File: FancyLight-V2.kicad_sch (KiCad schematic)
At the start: 40 parts, among them J1 PWR, Q1 IRLML2402, SW1 ONOFF, U1 SB6286, U2 TP4056, U3 TTP223-BA6, U4 DW01-P, U5 CJL8205A

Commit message: WIP
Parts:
- removed C6: 10pF (15pF), Capacitor_SMD:C_0805_2012Metric, symbol Device:C_Small
- removed C7: 0.1u, Capacitor_SMD:C_0805_2012Metric, symbol Device:C_Small
- removed J1: PWR, Connector_USB:USB_Micro-B_Molex_47346-0001, symbol Connector:USB_B_Micro
- removed R10: 470, Resistor_SMD:R_0805_2012Metric, symbol Device:R_Small
- removed R12: 100, Resistor_SMD:R_0805_2012Metric, symbol Device:R_Small
- removed R13: 1k, Resistor_SMD:R_0805_2012Metric, symbol Device:R_Small
- removed TP1: VBAT, TestPoint:TestPoint_Pad_1.5x1.5mm, symbol Connector:TestPoint
- removed TP2: GND, TestPoint:TestPoint_Pad_1.5x1.5mm, symbol Connector:TestPoint
- removed TP3: TOGGLE, TestPoint:TestPoint_Pad_1.5x1.5mm, symbol Connector:TestPoint
- removed TP4: SENSE, TestPoint:TestPoint_Pad_1.0x1.0mm, symbol Connector:TestPoint
- removed U3: TTP223-BA6, Package_TO_SOT_SMD:SOT-23-6, symbol TTP223-BA6:TTP223-BA6
- removed U4: DW01-P, Package_TO_SOT_SMD:SOT-23-6, symbol glebko:DW01-P
- removed U5: CJL8205A, Package_TO_SOT_SMD:TSOT-23-6, symbol glebko:CJL8205A
- added C3: 0.1u, Capacitor_SMD:C_0603_1608Metric, symbol Device:C_Small
- added D10: LED, LED_SMD:LED_0603_1608Metric, symbol Device:LED
- added D7, D8: MBR0520LT1, Diode_SMD:D_SOD-123, symbol Device:D_Schottky
- added D9: RB751V-40, Diode_SMD:D_SOD-323, symbol Device:D_Schottky
- added H1, H2, H3, H4: ~, MountingHole:MountingHole_2.5mm, symbol Mechanical:MountingHole
- added J2: TOUCH, Connector_PinHeader_1.27mm:PinHeader_1x03_P1.27mm_Vertical, symbol Connector:Conn_01x03_Pin
- added J2: ISP, Connector_PinHeader_2.54mm:PinHeader_2x03_P2.54mm_Vertical, symbol Connector_Generic:Conn_02x03_Odd_Even
- added J3: MODE, Connector_PinHeader_2.54mm:PinHeader_2x02_P2.54mm_Vertical, symbol Connector_Generic:Conn_02x02_Odd_Even
- added Q2: IRLML2402, Package_TO_SOT_SMD:SOT-23, symbol Device:Q_NMOS_GSD
- added R15: R_Photo, Connector_PinHeader_1.27mm:PinHeader_1x02_P1.27mm_Vertical, symbol Device:R_Photo
- added R17: 5k, Resistor_SMD:R_0603_1608Metric, symbol Device:R_Small
- added R2 (x3): 10k, Resistor_SMD:R_0603_1608Metric, symbol Device:R_Small
- added R2 (x2): 330, Resistor_SMD:R_0603_1608Metric, symbol Device:R_Small
- added RN1: 330, Resistor_SMD:R_Array_Convex_4x0603, symbol Device:R_Pack04
- added U3: XB3303A, kicad_lceda:SOT-23-3_L2.9-W1.3-P1.90-LS2.4-BR, symbol kicad_lceda:XB3303A
- added U5: syn480r, Connector_PinHeader_1.27mm:PinHeader_1x03_P1.27mm_Vertical, symbol rf:syn480r
- added U6: ATtiny44A-M, Package_DFN_QFN:QFN-20-1EP_4x4mm_P0.5mm_EP2.6x2.6mm, symbol MCU_Microchip_ATtiny:ATtiny44A-M
- added USB1: TYPE-C_6P, kicad_lceda:TYPE-C-SMD_TYPE-C-6P, symbol kicad_lceda:TYPE-C_6P
- BT1, SW1: footprint Connector_PinHeader_2.54mm:PinHeader_2x01_P2.54mm_Vertical -> Connector_PinHeader_1.27mm:PinHeader_1x02_P1.27mm_Vertical
- C3, C4: footprint Capacitor_SMD:C_0805_2012Metric -> Capacitor_SMD:C_0603_1608Metric
- C5: footprint Capacitor_SMD:C_0805_2012Metric -> Capacitor_SMD:C_0603_1608Metric; LCSC C49678 -> C15850
- D6: footprint LED_SMD:LED_1206_3216Metric -> LED_SMD:LED_0805_2012Metric
- R11, R3, R4, R5, R6: footprint Resistor_SMD:R_0805_2012Metric -> Resistor_SMD:R_0603_1608Metric
- R7: value 0 -> 5.1k; footprint Resistor_SMD:R_0805_2012Metric -> Resistor_SMD:R_0603_1608Metric; LCSC C304488 -> (none)
- R8: value 0 -> 1k; footprint Resistor_SMD:R_0805_2012Metric -> Resistor_SMD:R_0603_1608Metric; LCSC (none) -> C17513; now fitted; now in the parts list
- R9: value 0 -> 1k; footprint Resistor_SMD:R_0805_2012Metric -> Resistor_SMD:R_0603_1608Metric; LCSC C304488 -> C17513
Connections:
- net BAT+: now also R8.1, D8.2 (A); no longer SW1.1 (A)
- net GND: now also R7.2, R9.1, C3.1, D10.1 (K), J2.2 (Pin_2), J2.6 (Pin_6), Q2.2 (S), R2.1, U3.1 (VM), U6.21 (GND), U6.8 (GND), USB1.7 (EH), USB1.A12 (GND), USB1.B12 (GND); no longer C5.2, R9.2
- net VBAT: now also C3.2, J2.1 (Pin_1), J2.2 (Pin_2), R15.1, R2.2, U5.3 (VCC), U6.9 (VCC); no longer C5.1, R7.2, R8.1
- net PWM: now reaches Q1.1 (G), R11.1
- net PWM: now also RN1.6 (R3.2)
- net at R8.2: now also C5.1, U3.2 (VDD); no longer R9.1
- net at R7.1: now also USB1.A5 (CC1), USB1.B5 (CC2)
- net at BT1.2 (-): now also C5.2, U3.3 (GND)
- net TOGGLE renamed DCDC_EN
- net DCDC_EN: now also RN1.8 (R1.2)
- net VCC: no longer names the net of C3.1, D6.2 (A), U2.4 (VCC), U2.8 (CE)
- net VCC: now also R9.2, D7.2 (A), D9.2 (A), USB1.A9 (VBUS), USB1.B9 (VBUS)
- new net: D10.2 (A), R17.2
- new net: J3.2 (Pin_2), J3.4 (Pin_4), R2.2
- new net: Q2.3 (D), U5.1 (GND)
- new net: RN1.1 (R1.1), U6.5 (AREF/PA0)
- new net: RN1.2 (R2.1), U6.4 (PA1)
- new net: RN1.3 (R3.1), U6.3 (PA2)
- new net: RN1.4 (R4.1), U6.15 (PA7)
- new net: D7.1 (K), D8.1 (K), SW1.1 (A)
- new net: R2.1, U6.12 (XTAL2/PB1)
- new net: R15.2, R2.1, U6.2 (PA3)
- new net MISO: J2.1 (Pin_1), R2.2, U6.20 (PA5)
- new net MODE1: J2.4 (Pin_4), J3.1 (Pin_1), U6.16 (PA6)
- new net MODE2: J3.3 (Pin_3), U6.11 (XTAL1/PB0)
- new net RST: J2.5 (Pin_5), R2.1, U6.13 (~{RESET}/PB3)
- new net R_EN: Q2.1 (G), R2.1
- new net R_TRIG: RN1.5 (R4.2), U5.2 (DAT)
- new net SCK: J2.3 (Pin_3), R17.1, U6.1 (PA4)
- new net SENSE: D9.1 (K), R2.2
- new net SINK: R2.2, U6.14 (PB2)
- new net TRIG: J2.3 (Pin_3), RN1.7 (R2.2)
- no-connect marks 7 -> 1
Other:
- note removed: "P = U * I P = 6.4 * 0.084 = 0.54 Pd = I^2 * Rds Pd = 0.007 * 0.35 = 0.0025"
- note removed: "Vf = 3.2V If = 60 mA (max) Irec = If * 0.7 = 42 mA"
- moved on the sheet: BT1, C4, D1, D2, D3, D4, D6, Q1, R1, R11, R2, R6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

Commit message: Update CAD files and gitignore
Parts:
- J2, J3, L1, R15, USB1: now not fitted; now left out of the parts list
- U5: now left out of the parts list
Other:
- note added: "REMAP PWM PINs!!!!"
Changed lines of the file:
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@@
     (stroke (width 0) (type default))
+  )
+  (text "REMAP PWM PINs!!!!" (at 145.415 92.075 0)
+    (effects (font (size 2 2) (color 255 19 36 1)) (justify left bottom))
   )
   (text "400 mA\n" (at 24.765 121.285 0)
@@
   )
   (symbol (lib_id "LQH32MN2R2K23L:LQH32MN2R2K23L") (at 52.07 155.575 0) (unit 1)
-    (in_bom yes) (on_board yes) (dnp no) (fields_autoplaced)
+    (in_bom no) (on_board yes) (dnp yes) (fields_autoplaced)
     (property "Reference" "L1" (at 52.07 149.86 0)
       (effects (font (size 1.27 1.27)))
@@
   )
   (symbol (lib_id "rf:syn480r") (at 269.875 142.24 0) (unit 1)
-    (in_bom yes) (on_board yes) (dnp yes) (fields_autoplaced)
+    (in_bom no) (on_board yes) (dnp yes) (fields_autoplaced)
     (property "Reference" "U5" (at 270.51 132.08 0)
       (effects (font (size 1.27 1.27)))
@@
   )
   (symbol (lib_id "kicad_lceda:TYPE-C_6P") (at 30.48 61.595 0) (mirror y) (unit 1)
-    (in_bom yes) (on_board yes) (dnp no)
+    (in_bom no) (on_board yes) (dnp yes)
     (property "Reference" "USB1" (at 27.94 50.165 0)
       (effects (font (size 1.27 1.27)))
@@
   )
   (symbol (lib_id "Connector:Conn_01x03_Pin") (at 202.565 19.685 90) (mirror x) (unit 1)
-    (in_bom yes) (on_board yes) (dnp no)
+    (in_bom no) (on_board yes) (dnp yes)
     (property "Reference" "J2" (at 202.565 15.24 90)
       (effects (font (size 1.27 1.27)))
@@
   )
   (symbol (lib_id "Device:R_Photo") (at 270.51 48.895 0) (unit 1)
-    (in_bom yes) (on_board yes) (dnp no) (fields_autoplaced)
+    (in_bom no) (on_board yes) (dnp yes) (fields_autoplaced)
     (property "Reference" "R15" (at 273.05 48.26 0)
       (effects (font (size 1.27 1.27)) (justify left))
@@
   )
   (symbol (lib_id "Connector_Generic:Conn_02x03_Odd_Even") (at 151.13 177.546 0) (unit 1)
-    (in_bom yes) (on_board yes) (dnp no) (fields_autoplaced)
+    (in_bom no) (on_board yes) (dnp yes) (fields_autoplaced)
     (property "Reference" "J2" (at 152.4 169.926 0)
       (effects (font (size 1.27 1.27)))
@@
   )
   (symbol (lib_id "Connector_Generic:Conn_02x02_Odd_Even") (at 273.05 111.76 0) (unit 1)
-    (in_bom yes) (on_board yes) (dnp no) (fields_autoplaced)
+    (in_bom no) (on_board yes) (dnp yes) (fields_autoplaced)
     (property "Reference" "J3" (at 274.32 106.045 0)
       (effects (font (size 1.27 1.27)))

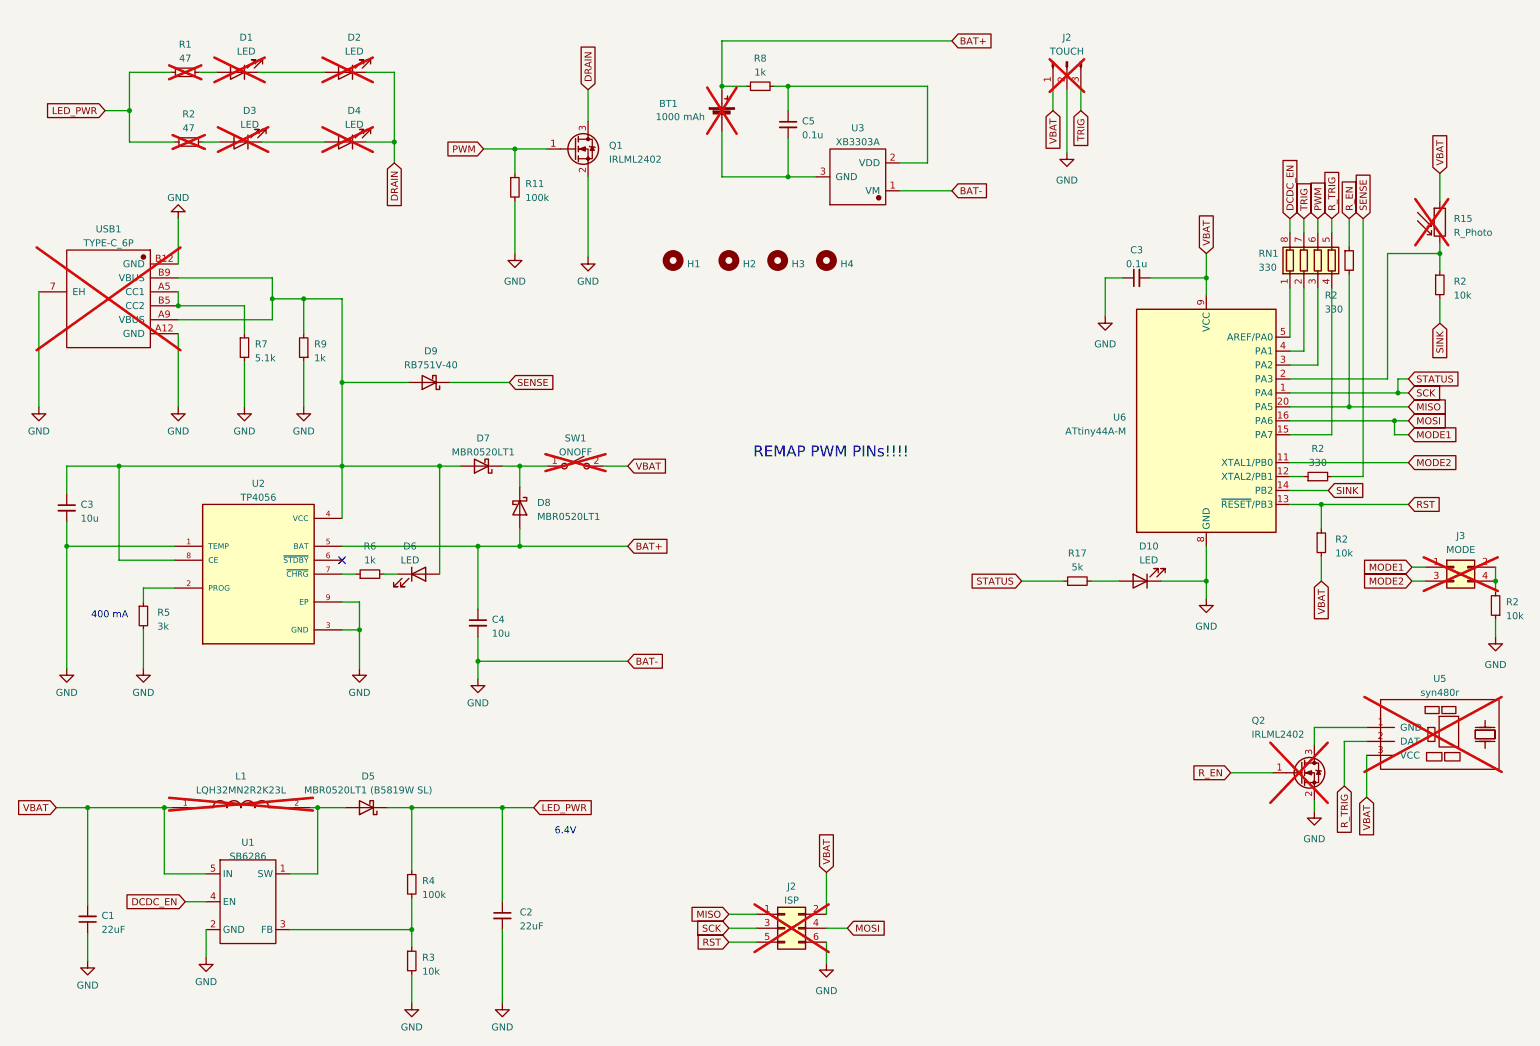
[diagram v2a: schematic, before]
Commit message: feat: Add power control, config, touch control, brightness control, and illumination control modules
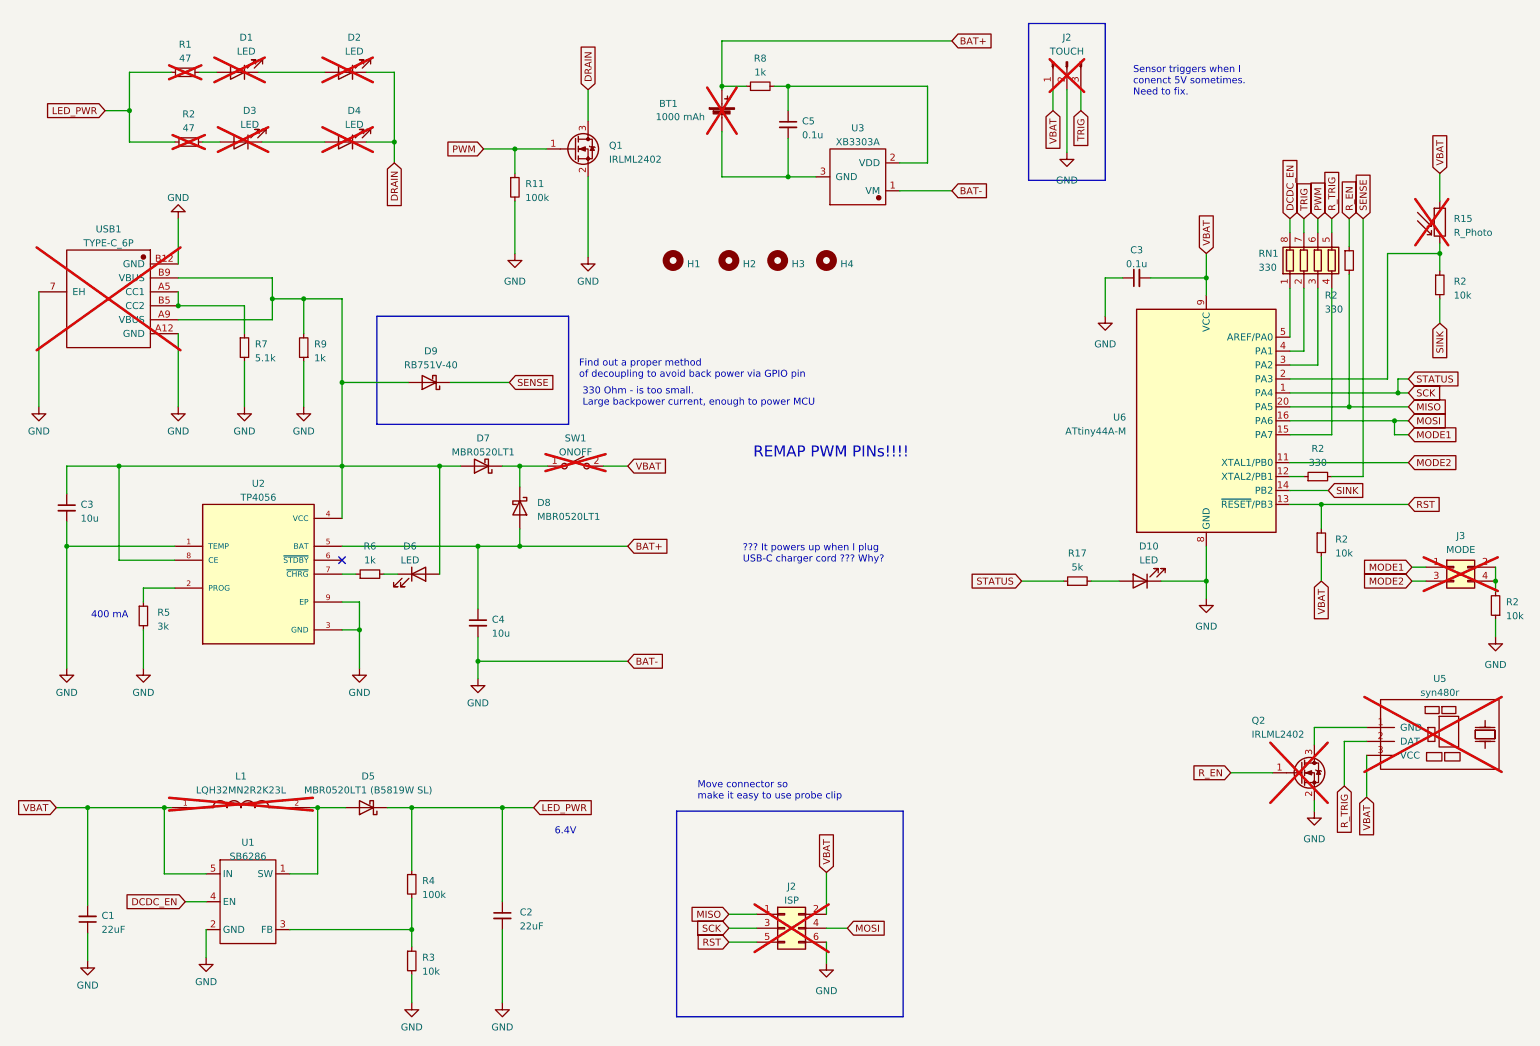
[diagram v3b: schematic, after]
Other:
- note added: "330 Ohm - is too small. Large backpower current, enough to power MCU"
- note added: "??? It powers up when I plug USB-C charger cord ??? Why?"
- note added: "Find out a proper method of decoupling to avoid back power via GPIO pin"
- note added: "Move connector so make it easy to use probe clip"
- note added: "Sensor triggers when I conenct 5V sometimes. Need to fix."
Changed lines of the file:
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@@
     (stroke (width 0) (type default))
+  )
+  (rectangle (start 195.58 12.7) (end 209.55 41.275)
+    (stroke (width 0) (type default))
+    (fill (type none))
+  )
+  (rectangle (start 76.835 66.04) (end 111.76 85.725)
+    (stroke (width 0) (type default))
+    (fill (type none))
+  )
+  (rectangle (start 131.445 156.21) (end 172.72 193.675)
+    (stroke (width 0) (type default))
+    (fill (type none))
+  )
+  (text "330 Ohm - is too small.\nLarge backpower current, enough to power MCU"
+    (at 114.3 82.55 0)
+    (effects (font (size 1.27 1.27)) (justify left bottom))
   )
   (text "REMAP PWM PINs!!!!" (at 145.415 92.075 0)
     (effects (font (size 2 2) (color 255 19 36 1)) (justify left bottom))
+  )
+  (text "Find out a proper method\nof decoupling to avoid back power via GPIO pin"
+    (at 113.665 77.47 0)
+    (effects (font (size 1.27 1.27)) (justify left bottom))
+  )
+  (text "??? It powers up when I plug \nUSB-C charger cord ??? Why?"
+    (at 143.51 111.125 0)
+    (effects (font (size 1.27 1.27)) (justify left bottom))
+  )
+  (text "Move connector so \nmake it easy to use probe clip" (at 135.255 154.305 0)
+    (effects (font (size 1.27 1.27)) (justify left bottom))
   )
   (text "400 mA\n" (at 24.765 121.285 0)
@@
     (effects (font (size 1.27 1.27)) (justify left bottom))
   )
+  (text "Sensor triggers when I\nconenct 5V sometimes.\nNeed to fix."
+    (at 214.63 26.035 0)
+    (effects (font (size 1.27 1.27)) (justify left bottom))
+  )

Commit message: Improve schematic and PCB
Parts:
- removed J2: ISP, Connector_PinHeader_2.54mm:PinHeader_2x03_P2.54mm_Vertical, symbol Connector_Generic:Conn_02x03_Odd_Even
- removed L1: LQH32MN2R2K23L, lib:IND_LQH32MN2R2K23L, symbol LQH32MN2R2K23L:LQH32MN2R2K23L
- removed R2: 330, Resistor_SMD:R_0603_1608Metric, symbol Device:R_Small
- added C5, C7, C8: 10u, Capacitor_SMD:C_0603_1608Metric, symbol Device:C_Small
- added H5: ~, MountingHole:MountingHole_2.1mm, symbol Mechanical:MountingHole
- added J1: ISP, Connector_PinHeader_2.54mm:PinHeader_2x03_P2.54mm_Vertical, symbol Connector_Generic:Conn_02x03_Odd_Even
- added Q1: AO3400A, Package_TO_SOT_SMD:SOT-23, symbol Device:Q_NMOS_GSD
- added R10, R11: 10k, Resistor_SMD:R_0603_1608Metric, symbol Device:R_Small
- added U1: APSWPA3015S4R7MTF, kicad_lceda:IND-SMD_L3.0-W3.0, symbol kicad_lceda:APSWPA3015S4R7MTF
- added U5: HT7530S_C5451677, kicad_lceda:SOT-23-3_L2.9-W1.3-P1.90-LS2.4-BR-CW, symbol kicad_lceda:HT7530S_C5451677
- C1: renamed from C3; LCSC C15850 -> C96446
- C2: renamed from C1; LCSC C398931 -> C45783
- C3: renamed from C4; LCSC C15850 -> C96446
- C3: LCSC (none) -> C14663
- C4: renamed from C2; LCSC C398931 -> C45783
- C6: renamed from C5; LCSC C15850 -> C14663
- D1, D4: LCSC (none) -> C210310; now fitted; now in the parts list
- D10: value LED -> STATUS LED; LCSC (none) -> C2286
- D2: renamed from D3; LCSC (none) -> C210310; now fitted; now in the parts list
- D3: renamed from D2; LCSC (none) -> C210310; now fitted; now in the parts list
- D5: value MBR0520LT1 (B5819W SL) -> B5819W SL
- D6: renamed from D9; value RB751V-40 -> 1N5819WS; LCSC (none) -> C191023
- D7: renamed from D6; value LED -> CHRG LED; footprint LED_SMD:LED_0805_2012Metric -> LED_SMD:LED_0603_1608Metric; LCSC C688886 -> C2286
- D8: renamed from D7; value MBR0520LT1 -> B5819W SL; LCSC (none) -> C8598
- D9: renamed from D8; value MBR0520LT1 -> B5819W SL; LCSC (none) -> C8598
- H1, H2, H3, H4: now not fitted; now left out of the parts list
- Q2: renamed from Q1; value IRLML2402 -> AO3400A; LCSC C5364307 -> C20917
- Q3: renamed from Q2; value IRLML2402 -> AO3400A; LCSC C5364307 -> C20917
- R1: renamed from R5; LCSC C17661 -> C4211
- R12: renamed from R8; LCSC C17513 -> C21190
- R13: renamed from R17; LCSC C17513 -> C23186
- R2: renamed from R1; value 47 -> 22; LCSC (none) -> C17561; now fitted; now in the parts list
- R2: LCSC (none) -> C25804
- R2: LCSC (none) -> C23138
- R3: renamed from R2; value 47 -> 22; LCSC (none) -> C17561; now fitted; now in the parts list
- R4: renamed from R7; LCSC (none) -> C23186
- R5: renamed from R9; LCSC C17513 -> C21190
- R6: LCSC C17513 -> C21190
- R7: renamed from R4; LCSC C149504 -> C25803
- R8: renamed from R3; LCSC C17414 -> C25804
- R9: renamed from R11; LCSC C149504 -> C25803
- RN1: value 330 -> 470; LCSC (none) -> C25510
- U4: renamed from U3; LCSC (none) -> C154937
- U6: LCSC (none) -> C123718
- USB1: LCSC (none) -> C456012; now fitted; now in the parts list
- renumbered R15 to R16, U1 to U2, U2 to U3, U5 to U7
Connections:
- net GND: now also C5.2, C7.2, C8.2, J1.6 (Pin_6), R11.2, U5.1 (GND)
- net MISO: now also J1.1 (Pin_1)
- net MODE1: now also J1.4 (Pin_4)
- net PWM: now also RN1.5 (R4.2); no longer RN1.6 (R3.2)
- net RST: now also J1.5 (Pin_5)
- net R_TRIG: now also RN1.6 (R3.2); no longer RN1.5 (R4.2)
- net SCK: now also J1.3 (Pin_3)
- net SENSE: now also U6.12 (XTAL2/PB1), R10.2, R11.1; no longer D6.1 (K)
- net VBAT: now also C5.1, J1.2 (Pin_2), Q1.1 (G), U1.1, U5.2 (VIN); no longer J2.1 (Pin_1), R16.1
- net at D5.2 (A), U2.1 (SW): now also U1.2
- net at RN1.3 (R3.1): now also U6.15 (PA7); no longer U6.3 (PA2)
- net at RN1.4 (R4.1): now also U6.14 (PB2); no longer U6.15 (PA7)
- net SINK: no longer names the net of R2.2
- net SINK: now also U6.3 (PA2); no longer U6.14 (PB2)
- new net: D6.1 (K), Q1.3 (D)
- new net: Q1.2 (S), R10.1
- new net 3V: C7.1, C8.1, J2.1 (Pin_1), R16.1, U5.3 (VOUT)
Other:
- note removed: "330 Ohm - is too small. Large backpower current, enough to power MCU"
- note removed: "??? It powers up when I plug USB-C charger cord ??? Why?"
- note removed: "Find out a proper method of decoupling to avoid back power via GPIO pin"
- note removed: "Move connector so make it easy to use probe clip"
- note removed: "REMAP PWM PINs!!!!"
- note removed: "Sensor triggers when I conenct 5V sometimes. Need to fix."
- moved on the sheet: D6, J2, Q2, R9
